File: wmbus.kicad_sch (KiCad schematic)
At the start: 26 parts, among them IC1 IM871A, J1 480-37-1000, J2 Conn_Coaxial, J3 Conn_01x04_Male, U1 USBLC6-2SC6, U2 XC6206P332MR, U3 CH340E

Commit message: Routing done
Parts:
- J2: footprint Connector_Coaxial:SMA_Amphenol_132289_EdgeMount -> wmbus:SMA-SMD_BWSMA-KE-P001
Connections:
- net GND: now also J2.3 (Ext), J2.4 (Ext), J2.5 (Ext)
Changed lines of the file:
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@@
   (junction (at 190.246 93.472) (diameter 0) (color 0 0 0 0)
   )
+  (junction (at 135.382 115.316) (diameter 0) (color 0 0 0 0)
+  )
   (junction (at 117.856 151.13) (diameter 0) (color 0 0 0 0)
   )
@@
   (junction (at 168.148 43.688) (diameter 0) (color 0 0 0 0)
   )
+  (junction (at 137.922 115.316) (diameter 0) (color 0 0 0 0)
+  )
   (junction (at 50.038 62.992) (diameter 0) (color 0 0 0 0)
   )
@@
   )
   (junction (at 193.294 43.688) (diameter 0) (color 0 0 0 0)
+  )
+  (junction (at 140.462 115.316) (diameter 0) (color 0 0 0 0)
   )
   (junction (at 157.734 43.688) (diameter 0) (color 0 0 0 0)
@@
     (stroke (width 0) (type default) (color 0 0 0 0))
   )
-  (wire (pts (xy 114.046 110.236) (xy 129.794 110.236))
-    (stroke (width 0) (type default) (color 0 0 0 0))
-  )
   (wire (pts (xy 127.508 112.776) (xy 127.508 113.792))
     (stroke (width 0) (type default) (color 0 0 0 0))
   )
+  (wire (pts (xy 114.046 110.236) (xy 131.572 110.236))
+    (stroke (width 0) (type default) (color 0 0 0 0))
+  )
   (polyline (pts (xy 34.798 165.608) (xy 34.798 100.838))
     (stroke (width 0) (type default) (color 0 0 0 0))
@@
     (stroke (width 0) (type default) (color 0 0 0 0))
   )
+  (wire (pts (xy 132.842 115.316) (xy 135.382 115.316))
+    (stroke (width 0) (type default) (color 0 0 0 0))
+  )
   (wire (pts (xy 157.734 51.054) (xy 157.734 56.5404))
     (stroke (width 0) (type default) (color 0 0 0 0))
@@
     (stroke (width 0) (type default) (color 0 0 0 0))
   )
+  (wire (pts (xy 137.922 115.316) (xy 140.462 115.316))
+    (stroke (width 0) (type default) (color 0 0 0 0))
+  )
   (wire (pts (xy 193.294 43.688) (xy 201.422 43.688))
     (stroke (width 0) (type default) (color 0 0 0 0))
@@
     (stroke (width 0) (type default) (color 0 0 0 0))
   )
-  (wire (pts (xy 134.874 115.316) (xy 134.874 116.586))
+  (wire (pts (xy 140.462 115.316) (xy 140.462 116.586))
     (stroke (width 0) (type default) (color 0 0 0 0))
   )
@@
   )
   (polyline (pts (xy 247.904 53.34) (xy 210.82 53.34))
+    (stroke (width 0) (type default) (color 0 0 0 0))
+  )
+  (wire (pts (xy 135.382 115.316) (xy 137.922 115.316))
     (stroke (width 0) (type default) (color 0 0 0 0))
   )
@@
     (pin "2")
   )
-  (symbol (lib_id "Connector:Conn_Coaxial") (at 134.874 110.236 0) (unit 1)
-    (in_bom yes) (on_board yes) (fields_autoplaced)
-    (property "Reference" "J2" (id 0) (at 138.43 109.2591 0)
-      (effects (font (size 1.27 1.27)) (justify left))
-    )
-    (property "Value" "Conn_Coaxial" (id 1) (at 138.43 111.7991 0)
-      (effects (font (size 1.27 1.27)) (justify left))
-    )
-    (property "Footprint" "Connector_Coaxial:SMA_Amphenol_132289_EdgeMount" (id 2) (at 134.874 110.236 0)
-      (effects (font (size 1.27 1.27)) hide)
-    )
-    (property "Datasheet" " ~" (id 3) (at 134.874 110.236 0)
-      (effects (font (size 1.27 1.27)) hide)
-    )
-    (pin "1")
-    (pin "2")
+  (symbol (lib_id "Connector:Conn_Coaxial") (at 136.652 110.236 0) (unit 1)
+    (in_bom yes) (on_board yes) (fields_autoplaced)
+    (property "Reference" "J2" (id 0) (at 140.208 109.2591 0)
+      (effects (font (size 1.27 1.27)) (justify left))
+    )
+    (property "Value" "Conn_Coaxial" (id 1) (at 140.208 111.7991 0)
+      (effects (font (size 1.27 1.27)) (justify left))
+    )
+    (property "Footprint" "wmbus:SMA-SMD_BWSMA-KE-P001" (id 2) (at 136.652 110.236 0)
+      (effects (font (size 1.27 1.27)) hide)
+    )
+    (property "Datasheet" " ~" (id 3) (at 136.652 110.236 0)
+      (effects (font (size 1.27 1.27)) hide)
+    )
+    (pin "1")
+    (pin "2")
+    (pin "3")
+    (pin "4")
+    (pin "5")
   )
   (symbol (lib_id "Device:LED_Small") (at 43.942 120.904 90) (unit 1)
@@
     (pin "9")
   )
-  (symbol (lib_id "power:GND") (at 134.874 116.586 0) (unit 1)
-    (in_bom yes) (on_board yes) (fields_autoplaced)
-    (property "Reference" "#PWR017" (id 0) (at 134.874 122.936 0)
-      (effects (font (size 1.27 1.27)) hide)
-    )
-    (property "Value" "GND" (id 1) (at 134.874 122.174 0)
-      (effects (font (size 1.27 1.27)) hide)
-    )
-    (property "Footprint" "" (id 2) (at 134.874 116.586 0)
-      (effects (font (size 1.27 1.27)) hide)
-    )
-    (property "Datasheet" "" (id 3) (at 134.874 116.586 0)
+  (symbol (lib_id "power:GND") (at 140.462 116.586 0) (unit 1)
+    (in_bom yes) (on_board yes) (fields_autoplaced)
+    (property "Reference" "#PWR017" (id 0) (at 140.462 122.936 0)
+      (effects (font (size 1.27 1.27)) hide)
+    )
+    (property "Value" "GND" (id 1) (at 140.462 122.174 0)
+      (effects (font (size 1.27 1.27)) hide)
+    )
+    (property "Footprint" "" (id 2) (at 140.462 116.586 0)
+      (effects (font (size 1.27 1.27)) hide)
+    )
+    (property "Datasheet" "" (id 3) (at 140.462 116.586 0)
       (effects (font (size 1.27 1.27)) hide)
     )
@@
     )
     (path "/e6b81e0e-a2cc-422b-a7a0-32e56b2495ae"
-      (reference "J2") (unit 1) (value "Conn_Coaxial") (footprint "Connector_Coaxial:SMA_Amphenol_132289_EdgeMount")
+      (reference "J2") (unit 1) (value "Conn_Coaxial") (footprint "wmbus:SMA-SMD_BWSMA-KE-P001")
     )
     (path "/165310ef-1002-45f5-bb06-d3332e8c0024"

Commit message: Ready for production rev1
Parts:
- IC1: footprint IM871A -> wmbus:IM871A
- J1: footprint MOLEX_480-37-1000 -> wmbus:MOLEX_480-37-1000
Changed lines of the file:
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@@
     (property "Reference" "IC1" (id 0) (at 94.996 102.87 0))
     (property "Value" "IM871A" (id 1) (at 94.996 105.41 0))
-    (property "Footprint" "IM871A" (id 2) (at 110.236 107.696 0)
+    (property "Footprint" "wmbus:IM871A" (id 2) (at 110.236 107.696 0)
       (effects (font (size 1.27 1.27)) (justify left) hide)
     )
@@
     (property "Reference" "J1" (id 0) (at 35.814 40.64 0))
     (property "Value" "480-37-1000" (id 1) (at 35.814 43.18 0))
-    (property "Footprint" "MOLEX_480-37-1000" (id 2) (at 35.814 53.086 0)
+    (property "Footprint" "wmbus:MOLEX_480-37-1000" (id 2) (at 35.814 53.086 0)
       (effects (font (size 1.27 1.27)) (justify left bottom) hide)
     )
@@
     )
     (path "/0ad72dfe-4dba-4409-bc67-734cd14155b9"
-      (reference "IC1") (unit 1) (value "IM871A") (footprint "IM871A")
+      (reference "IC1") (unit 1) (value "IM871A") (footprint "wmbus:IM871A")
     )
     (path "/3f0ee482-312c-4799-b9be-0ee983b048cc"
-      (reference "J1") (unit 1) (value "480-37-1000") (footprint "MOLEX_480-37-1000")
+      (reference "J1") (unit 1) (value "480-37-1000") (footprint "wmbus:MOLEX_480-37-1000")
     )
     (path "/e6b81e0e-a2cc-422b-a7a0-32e56b2495ae"

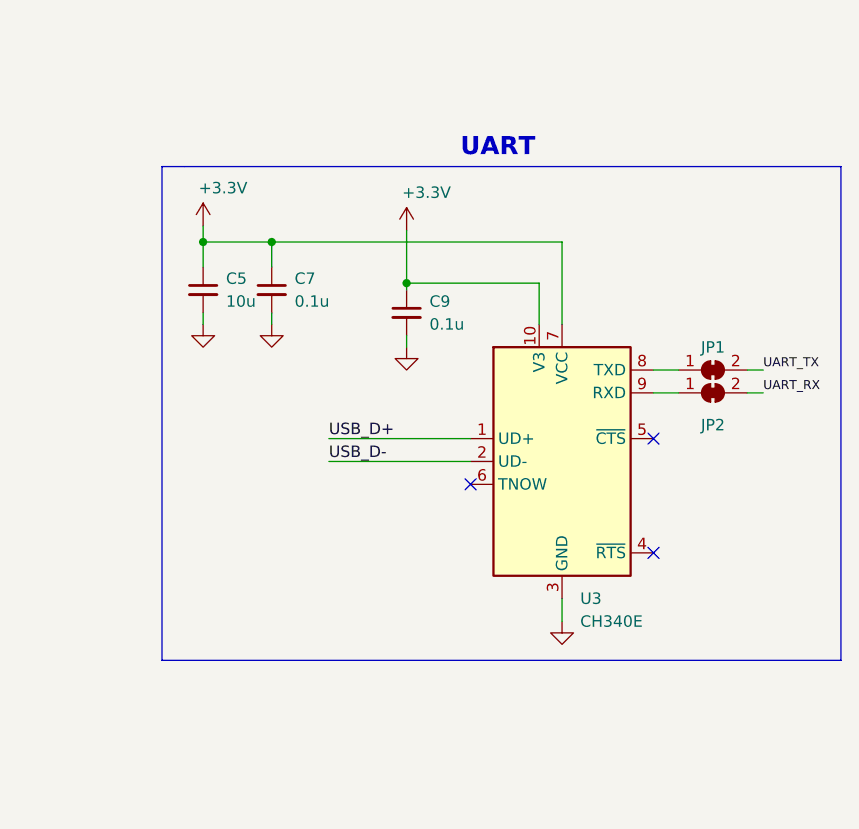
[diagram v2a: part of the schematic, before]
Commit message: rev2 - smaller, removed unused rx/tx jumpers
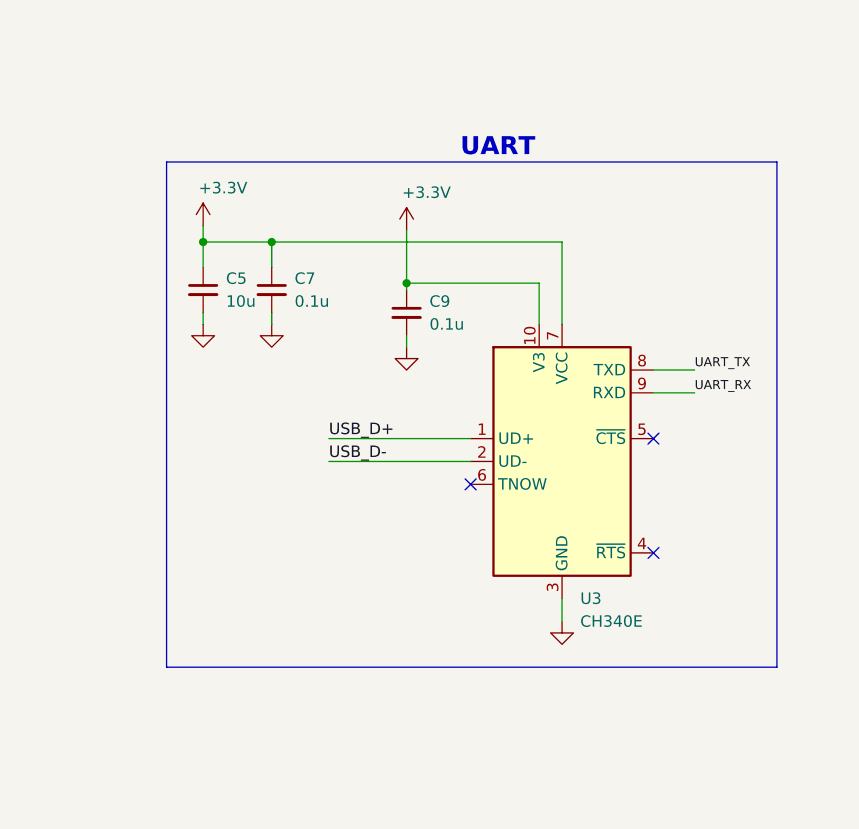
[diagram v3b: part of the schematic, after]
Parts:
- removed JP1, JP2: SolderJumper_2_Bridged, Jumper:SolderJumper-2_P1.3mm_Bridged_RoundedPad1.0x1.5mm, symbol Jumper:SolderJumper_2_Bridged
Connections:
- net UART_RX: now also U3.9 (RXD)
- net UART_TX: now also U3.8 (TXD)
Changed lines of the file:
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@@
   (title_block
     (title "WM-BUS to USB converter")
-    (date "2022-11-01")
-    (rev "1.0")
+    (date "2022-11-21")
+    (rev "2.0")
     (company "Jan Gnip")
   )
@@
     (stroke (width 0) (type default) (color 0 0 0 0))
   )
-  (polyline (pts (xy 185.674 85.09) (xy 188.214 85.09))
-    (stroke (width 0) (type default) (color 0 0 0 0))
-  )
   (wire (pts (xy 201.422 51.054) (xy 201.422 56.5404))
     (stroke (width 0) (type default) (color 0 0 0 0))
@@
     (stroke (width 0) (type default) (color 0 0 0 0))
   )
+  (polyline (pts (xy 254 84.582) (xy 254 140.716))
+    (stroke (width 0) (type default) (color 0 0 0 0))
+  )
   (wire (pts (xy 212.852 92.202) (xy 212.852 98.044))
     (stroke (width 0) (type default) (color 0 0 0 0))
@@
     (stroke (width 0) (type default) (color 0 0 0 0))
   )
-  (wire (pts (xy 250.698 107.696) (xy 252.476 107.696))
-    (stroke (width 0) (type default) (color 0 0 0 0))
-  )
   (wire (pts (xy 45.974 53.086) (xy 59.944 53.086))
     (stroke (width 0) (type default) (color 0 0 0 0))
@@
     (stroke (width 0) (type default) (color 0 0 0 0))
   )
-  (polyline (pts (xy 185.674 139.954) (xy 185.674 85.09))
-    (stroke (width 0) (type default) (color 0 0 0 0))
-  )
-  (polyline (pts (xy 261.112 139.954) (xy 185.674 139.954))
-    (stroke (width 0) (type default) (color 0 0 0 0))
-  )
   (wire (pts (xy 132.842 115.316) (xy 135.382 115.316))
     (stroke (width 0) (type default) (color 0 0 0 0))
@@
     (stroke (width 0) (type default) (color 0 0 0 0))
   )
+  (polyline (pts (xy 186.182 84.582) (xy 186.182 140.716))
+    (stroke (width 0) (type default) (color 0 0 0 0))
+  )
   (wire (pts (xy 226.568 44.196) (xy 240.03 44.196))
     (stroke (width 0) (type default) (color 0 0 0 0))
@@
     (stroke (width 0) (type default) (color 0 0 0 0))
   )
-  (polyline (pts (xy 261.112 85.09) (xy 261.112 139.954))
-    (stroke (width 0) (type default) (color 0 0 0 0))
-  )
   (polyline (pts (xy 127.254 33.782) (xy 197.612 33.782))
     (stroke (width 0) (type default) (color 0 0 0 0))
   )
-  (wire (pts (xy 240.284 107.696) (xy 243.078 107.696))
+  (wire (pts (xy 240.284 107.696) (xy 244.856 107.696))
     (stroke (width 0) (type default) (color 0 0 0 0))
   )
@@
     (stroke (width 0) (type default) (color 0 0 0 0))
   )
+  (polyline (pts (xy 254 140.716) (xy 186.182 140.716))
+    (stroke (width 0) (type default) (color 0 0 0 0))
+  )
   (wire (pts (xy 193.294 43.688) (xy 193.294 45.974))
     (stroke (width 0) (type default) (color 0 0 0 0))
@@
     (stroke (width 0) (type default) (color 0 0 0 0))
   )
-  (wire (pts (xy 240.284 110.236) (xy 243.078 110.236))
+  (wire (pts (xy 240.284 110.236) (xy 244.856 110.236))
     (stroke (width 0) (type default) (color 0 0 0 0))
   )
@@
     (stroke (width 0) (type default) (color 0 0 0 0))
   )
-  (wire (pts (xy 250.698 110.236) (xy 252.476 110.236))
-    (stroke (width 0) (type default) (color 0 0 0 0))
-  )
   (wire (pts (xy 212.852 103.886) (xy 212.852 105.156))
     (stroke (width 0) (type default) (color 0 0 0 0))
@@
     (stroke (width 0) (type default) (color 0 0 0 0))
   )
-  (polyline (pts (xy 188.214 85.09) (xy 261.112 85.09))
-    (stroke (width 0) (type default) (color 0 0 0 0))
-  )
   (wire (pts (xy 188.468 43.688) (xy 193.294 43.688))
+    (stroke (width 0) (type default) (color 0 0 0 0))
+  )
+  (polyline (pts (xy 186.182 84.582) (xy 254 84.582))
     (stroke (width 0) (type default) (color 0 0 0 0))
   )
@@
     (effects (font (size 1.27 1.27)) (justify right bottom))
   )
-  (label "UART_TX" (at 252.476 107.696 0)
+  (label "UART_TX" (at 244.856 107.696 0)
     (effects (font (size 1 1)) (justify left bottom))
   )
@@
     (effects (font (size 1.27 1.27)) (justify left bottom))
   )
-  (label "UART_RX" (at 252.476 110.236 0)
+  (label "UART_RX" (at 244.856 110.236 0)
     (effects (font (size 1 1)) (justify left bottom))
   )
@@
     (pin "2")
   )
-  (symbol (lib_id "Jumper:SolderJumper_2_Bridged") (at 246.888 110.236 0) (unit 1)
-    (in_bom yes) (on_board yes)
-    (property "Reference" "JP2" (id 0) (at 246.888 114.554 0)
-      (effects (font (size 1.27 1.27)) (justify bottom))
-    )
-    (property "Value" "SolderJumper_2_Bridged" (id 1) (at 246.888 107.188 0)
-      (effects (font (size 1.27 1.27)) hide)
-    )
-    (property "Footprint" "Jumper:SolderJumper-2_P1.3mm_Bridged_RoundedPad1.0x1.5mm" (id 2) (at 246.888 110.236 0)
-      (effects (font (size 1.27 1.27)) hide)
-    )
-    (property "Datasheet" "~" (id 3) (at 246.888 110.236 0)
-      (effects (font (size 1.27 1.27)) hide)
-    )
-    (pin "1")
-    (pin "2")
-  )
   (symbol (lib_id "power:GND") (at 54.102 132.334 0) (unit 1)
     (in_bom yes) (on_board yes) (fields_autoplaced)
@@
     (pin "1")
   )
-  (symbol (lib_id "Jumper:SolderJumper_2_Bridged") (at 246.888 107.696 0) (unit 1)
-    (in_bom yes) (on_board yes)
-    (property "Reference" "JP1" (id 0) (at 246.888 105.918 0)
-      (effects (font (size 1.27 1.27)) (justify bottom))
-    )
-    (property "Value" "SolderJumper_2_Bridged" (id 1) (at 246.888 104.648 0)
-      (effects (font (size 1.27 1.27)) hide)
-    )
-    (property "Footprint" "Jumper:SolderJumper-2_P1.3mm_Bridged_RoundedPad1.0x1.5mm" (id 2) (at 246.888 107.696 0)
-      (effects (font (size 1.27 1.27)) hide)
-    )
-    (property "Datasheet" "~" (id 3) (at 246.888 107.696 0)
-      (effects (font (size 1.27 1.27)) hide)
-    )
-    (pin "1")
-    (pin "2")
-  )
   (sheet_instances
     (path "/" (page "1"))
@@
       (reference "J3") (unit 1) (value "Conn_01x04_Male") (footprint "Connector_PinHeader_2.54mm:PinHeader_1x04_P2.54mm_Vertical")
     )
-    (path "/ffb6248d-8a4d-49c2-bbbe-e85eb307179e"
-      (reference "JP1") (unit 1) (value "SolderJumper_2_Bridged") (footprint "Jumper:SolderJumper-2_P1.3mm_Bridged_RoundedPad1.0x1.5mm")
-    )
-    (path "/2e9d95f7-3531-4d3d-9cee-4c5fc1a0789f"
-      (reference "JP2") (unit 1) (value "SolderJumper_2_Bridged") (footprint "Jumper:SolderJumper-2_P1.3mm_Bridged_RoundedPad1.0x1.5mm")
-    )
     (path "/edbef5b1-e9cf-4449-ae34-cebaf37664cf"
